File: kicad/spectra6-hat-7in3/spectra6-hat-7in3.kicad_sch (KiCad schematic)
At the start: 0 parts

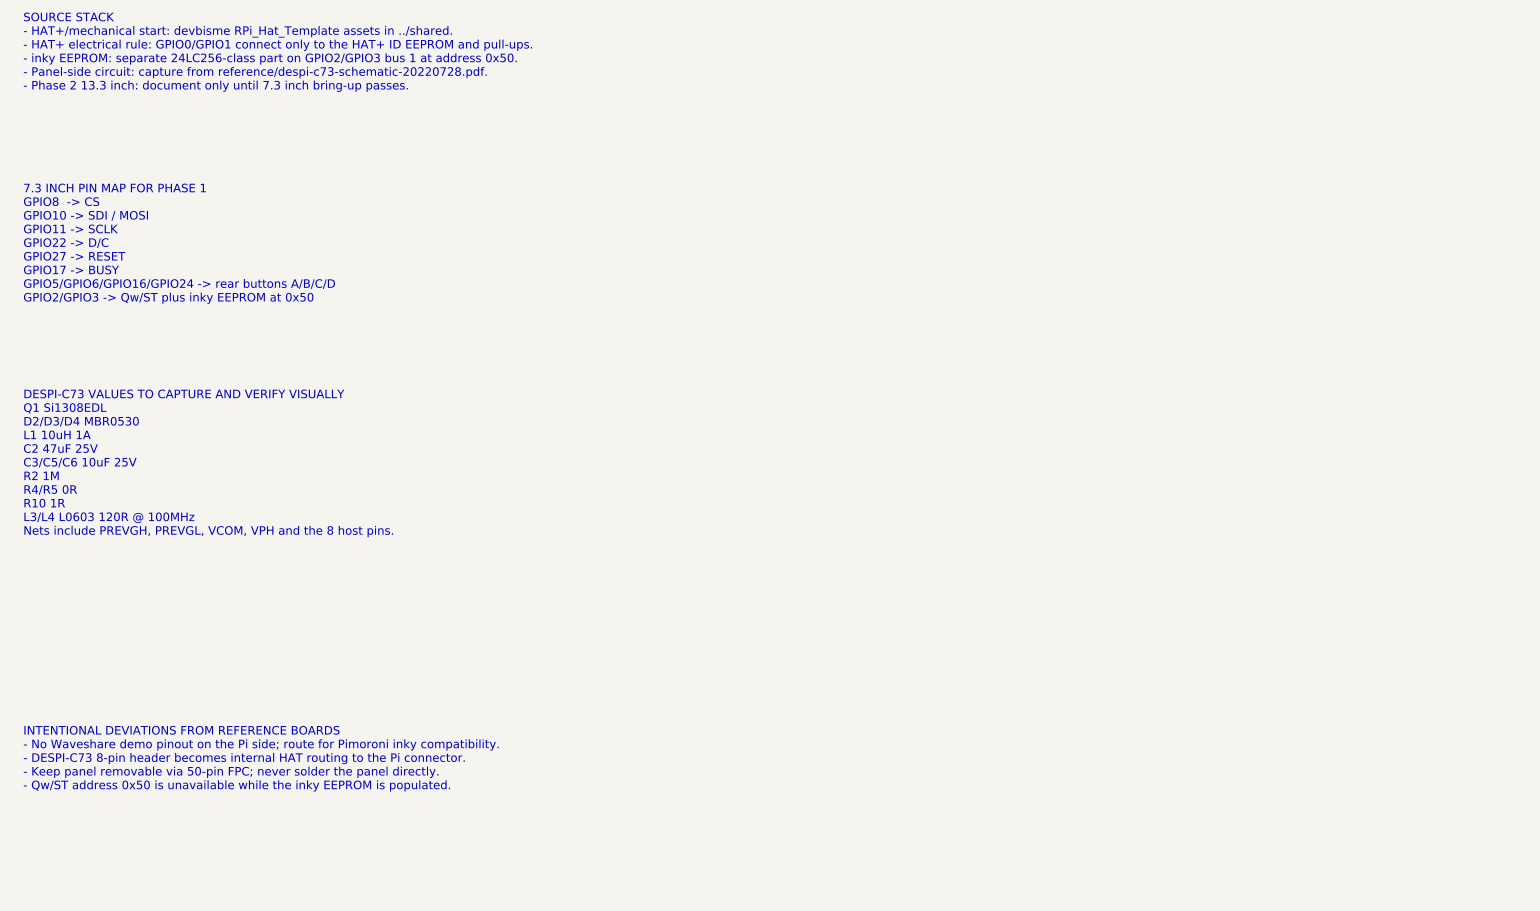
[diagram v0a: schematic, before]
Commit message: Capture Pi-side schematic blocks
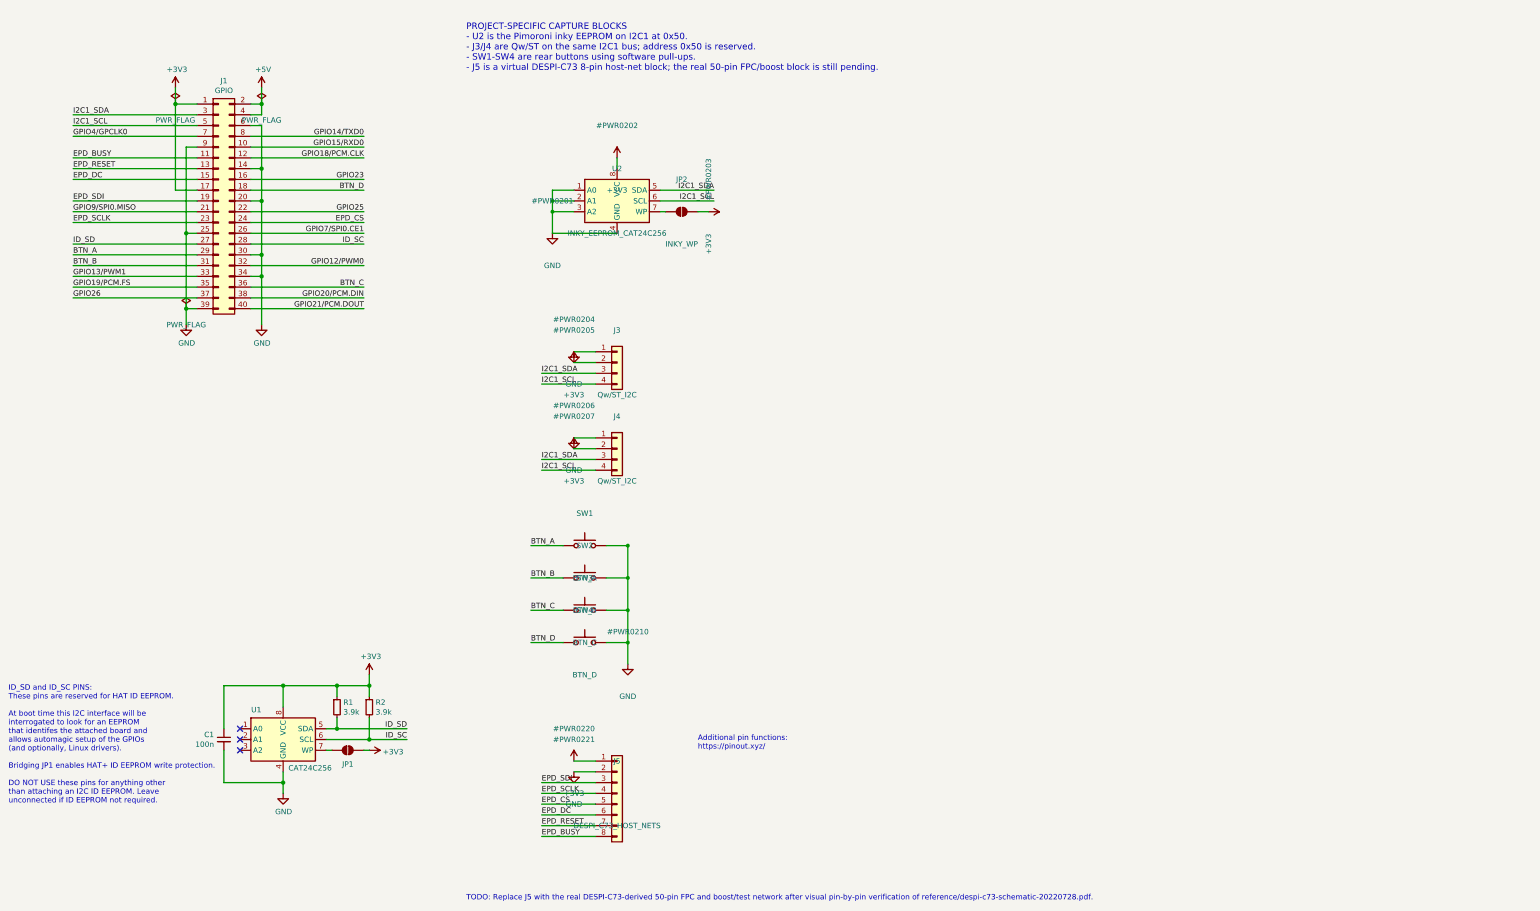
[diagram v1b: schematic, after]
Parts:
- added C1: 100n, symbol Device:C_Small
- added J1: GPIO, Connector_PinSocket_2.54mm:PinSocket_2x20_P2.54mm_Vertical, symbol Connector_Generic:Conn_02x20_Odd_Even
- added J3, J4: Qw/ST_I2C, Connector_JST:JST_SH_SM04B-SRSS-TB_1x04-1MP_P1.00mm_Horizontal, symbol Connector_Generic:Conn_01x04
- added J5: DESPI_C73_HOST_NETS, symbol Connector_Generic:Conn_01x08
- added JP1: ID_WP, symbol Jumper:SolderJumper_2_Open
- added JP2: INKY_WP, Jumper:SolderJumper-2_P1.3mm_Open_TrianglePad1.0x1.5mm, symbol Jumper:SolderJumper_2_Open
- added R1, R2: 3.9k, symbol Device:R_Small
- added SW1: BTN_A, symbol Switch:SW_Push
- added SW2: BTN_B, symbol Switch:SW_Push
- added SW3: BTN_C, symbol Switch:SW_Push
- added SW4: BTN_D, symbol Switch:SW_Push
- added U1: CAT24C256, symbol Memory_EEPROM:CAT24C256
- added U2: INKY_EEPROM_CAT24C256, Package_SO:SOIC-8_3.9x4.9mm_P1.27mm, symbol Memory_EEPROM:CAT24C256
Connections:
- new net: JP1.1 (A), U1.7 (WP)
- new net: JP2.1 (A), U2.7 (WP)
- new net +3V3: C1.1, J1.1 (Pin_1), J1.17 (Pin_17), J3.2 (Pin_2), J4.2 (Pin_2), J5.1 (Pin_1), JP1.2 (B), JP2.2 (B), R1.1, R2.1, U1.8 (VCC), U2.8 (VCC)
- new net +5V: J1.2 (Pin_2), J1.4 (Pin_4)
- new net BTN_A: J1.29 (Pin_29), SW1.1
- new net BTN_B: J1.31 (Pin_31), SW2.1
- new net BTN_C: J1.36 (Pin_36), SW3.1
- new net BTN_D: J1.18 (Pin_18), SW4.1
- new net EPD_BUSY: J1.11 (Pin_11), J5.8 (Pin_8)
- new net EPD_CS: J1.24 (Pin_24), J5.5 (Pin_5)
- new net EPD_DC: J1.15 (Pin_15), J5.6 (Pin_6)
- new net EPD_RESET: J1.13 (Pin_13), J5.7 (Pin_7)
- new net EPD_SCLK: J1.23 (Pin_23), J5.4 (Pin_4)
- new net EPD_SDI: J1.19 (Pin_19), J5.3 (Pin_3)
- new net GND: C1.2, J1.14 (Pin_14), J1.20 (Pin_20), J1.25 (Pin_25), J1.30 (Pin_30), J1.34 (Pin_34), J1.39 (Pin_39), J1.6 (Pin_6), J1.9 (Pin_9), J3.1 (Pin_1), J4.1 (Pin_1), J5.2 (Pin_2), SW1.2, SW2.2, SW3.2, SW4.2, U1.4 (GND), U2.1 (A0), U2.2 (A1), U2.3 (A2), U2.4 (GND)
- new net GPIO12/PWM0: J1.32 (Pin_32)
- new net GPIO13/PWM1: J1.33 (Pin_33)
- new net GPIO14/TXD0: J1.8 (Pin_8)
- new net GPIO15/RXD0: J1.10 (Pin_10)
- new net GPIO18/PCM.CLK: J1.12 (Pin_12)
- new net GPIO19/PCM.FS: J1.35 (Pin_35)
- new net GPIO20/PCM.DIN: J1.38 (Pin_38)
- new net GPIO21/PCM.DOUT: J1.40 (Pin_40)
- new net GPIO23: J1.16 (Pin_16)
- new net GPIO25: J1.22 (Pin_22)
- new net GPIO26: J1.37 (Pin_37)
- new net GPIO4/GPCLK0: J1.7 (Pin_7)
- new net GPIO7/SPI0.CE1: J1.26 (Pin_26)
- new net GPIO9/SPI0.MISO: J1.21 (Pin_21)
- new net I2C1_SCL: J1.5 (Pin_5), J3.4 (Pin_4), J4.4 (Pin_4), U2.6 (SCL)
- new net I2C1_SDA: J1.3 (Pin_3), J3.3 (Pin_3), J4.3 (Pin_3), U2.5 (SDA)
- new net ID_SC: J1.28 (Pin_28), R2.2, U1.6 (SCL)
- new net ID_SD: J1.27 (Pin_27), R1.2, U1.5 (SDA)
- no-connect marks 0 -> 3
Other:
- note added: "Additional pin functions: https://pinout.xyz/"
- note added: "ID_SD and ID_SC PINS: These pins are reserved for HAT ID EEPROM. At boot time this I2C interface will be interrogated to look for an EEPROM that identifes the attached board and allows automagic setup of the GPIOs (and optionally, Linux drivers). Bridging JP1 enables HAT+ ID EEPROM write protection. DO NOT USE these pins for anything other than attaching an I2C ID EEPROM. Leave unconnected if ID 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"
- note added: "PROJECT-SPECIFIC CAPTURE BLOCKS - U2 is the Pimoroni inky EEPROM on I2C1 at 0x50. - J3/J4 are Qw/ST on the same I2C1 bus; address 0x50 is reserved. - SW1-SW4 are rear buttons using software pull-ups. - J5 is a virtual DESPI-C73 8-pin host-net block; the real 50-pin FPC/boost block is still pending."
- note added: "TODO: Replace J5 with the real DESPI-C73-derived 50-pin FPC and boost/test network after visual pin-by-pin verification of reference/despi-c73-schematic-20220728.pdf."
- note removed: "7.3 INCH PIN MAP FOR PHASE 1 GPIO8 -> CS GPIO10 -> SDI / MOSI GPIO11 -> SCLK GPIO22 -> D/C GPIO27 -> RESET GPIO17 -> BUSY GPIO5/GPIO6/GPIO16/GPIO24 -> rear buttons A/B/C/D GPIO2/GPIO3 -> Qw/ST plus inky EEPROM at 0x50"
- note removed: "DESPI-C73 VALUES TO CAPTURE AND VERIFY VISUALLY Q1 Si1308EDL D2/D3/D4 MBR0530 L1 10uH 1A C2 47uF 25V C3/C5/C6 10uF 25V R2 1M R4/R5 0R R10 1R L3/L4 L0603 120R @ 100MHz Nets include PREVGH, PREVGL, VCOM, VPH and the 8 host pins."
- note removed: "INTENTIONAL DEVIATIONS FROM REFERENCE BOARDS - No Waveshare demo pinout on the Pi side; route for Pimoroni inky compatibility. - DESPI-C73 8-pin header becomes internal HAT routing to the Pi connector. - Keep panel removable via 50-pin FPC; never solder the panel directly. - Qw/ST address 0x50 is unavailable while the inky EEPROM is populated."
- note removed: "SOURCE STACK - HAT+/mechanical start: devbisme RPi_Hat_Template assets in ../shared. - HAT+ electrical rule: GPIO0/GPIO1 connect only to the HAT+ ID EEPROM and pull-ups. - inky EEPROM: separate 24LC256-class part on GPIO2/GPIO3 bus 1 at address 0x50. - Panel-side circuit: capture from reference/despi-c73-schematic-20220728.pdf. - Phase 2 13.3 inch: document only until 7.3 inch bring-up passes."
- title: Spectra 6 HAT 7.3 - Schematic Capture Prep -> Spectra 6 HAT 7.3 - Phase 1 Schematic

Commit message: Capture DESPI-C73 panel-side schematic
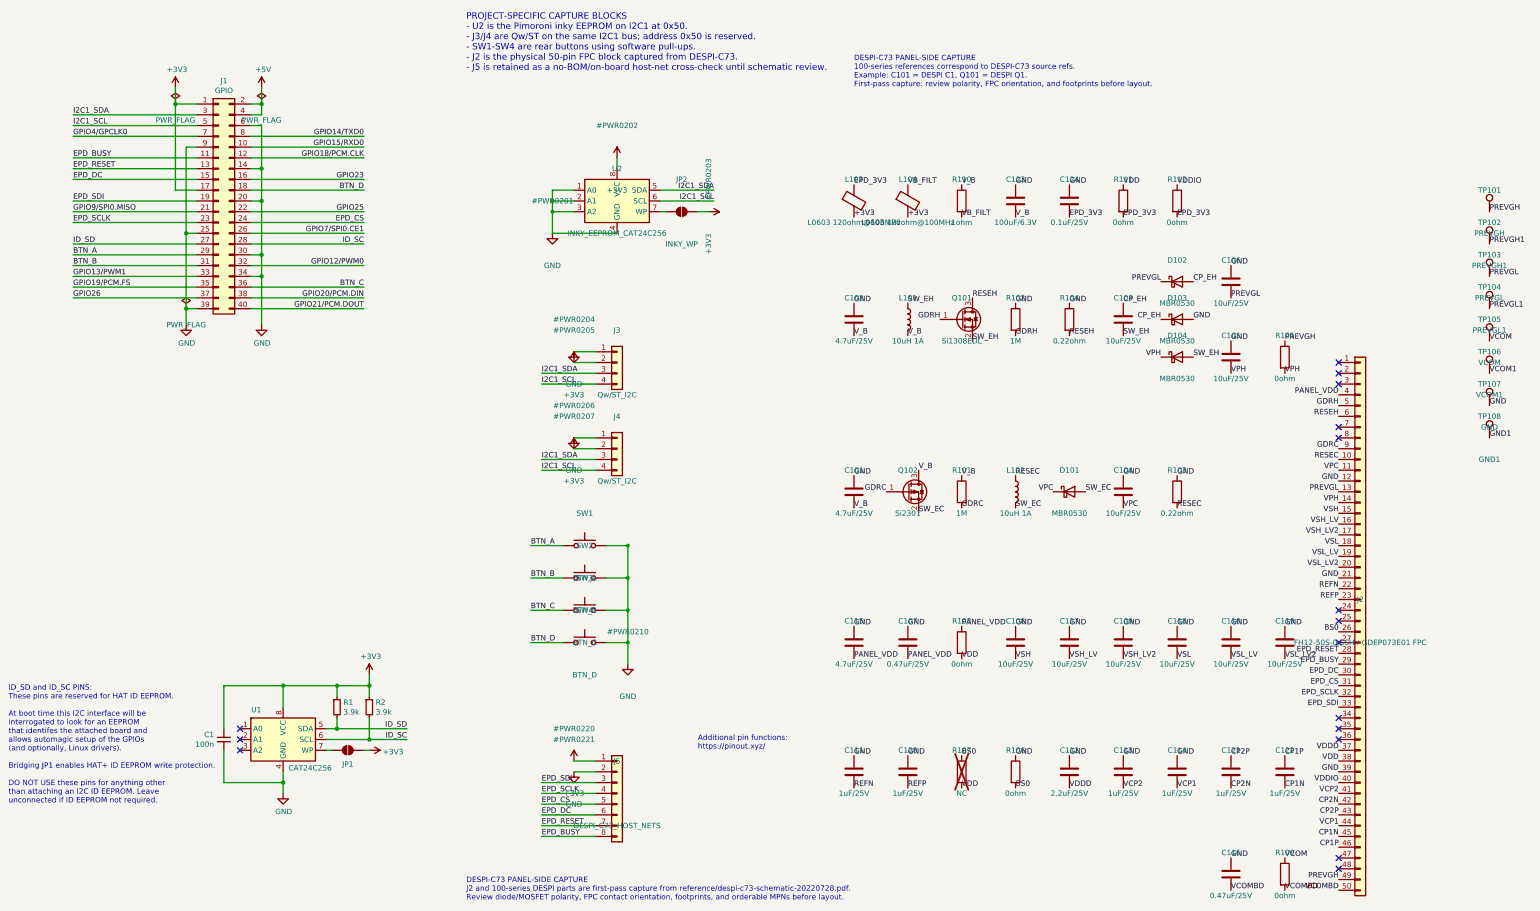
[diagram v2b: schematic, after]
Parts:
- added C101, C102, C115: 4.7uF/25V, symbol Device:C
- added C103, C104, C105, C106, C108, C109, C110, C117, C118, C119: 10uF/25V, symbol Device:C
- added C107, C116: 0.47uF/25V, symbol Device:C
- added C111, C113, C114, C120, C121, C122: 1uF/25V, symbol Device:C
- added C112: 2.2uF/25V, symbol Device:C
- added C123: 100uF/6.3V, symbol Device:C
- added C124: 0.1uF/25V, symbol Device:C
- added D101, D102, D103, D104: MBR0530, symbol Device:D_Schottky
- added J2: FH12-50S-0.5SH / GDEP073E01 FPC, Connector_FFC-FPC:Hirose_FH12-50S-0.5SH_1x50-1MP_P0.50mm_Horizontal, symbol Connector_Generic:Conn_01x50
- added L101, L102: 10uH 1A, symbol Device:L
- added L103, L104: L0603 120ohm@100MHz, symbol Device:FerriteBead
- added Q101: Si1308EDL, symbol Transistor_FET:Q_NMOS_GSD
- added Q102: Si2301, symbol Transistor_FET:Q_PMOS_GSD
- added R101, R102: 1M, symbol Device:R
- added R103, R104: 0.22ohm, symbol Device:R
- added R105, R106, R108, R109, R111, R112: 0ohm, symbol Device:R
- added R107: NC, symbol Device:R
- added R110: 1ohm, symbol Device:R
- added TP101: PREVGH, TestPoint:TestPoint_Pad_D1.0mm, symbol Connector:TestPoint
- added TP102: PREVGH1, TestPoint:TestPoint_Pad_D1.0mm, symbol Connector:TestPoint
- added TP103: PREVGL, TestPoint:TestPoint_Pad_D1.0mm, symbol Connector:TestPoint
- added TP104: PREVGL1, TestPoint:TestPoint_Pad_D1.0mm, symbol Connector:TestPoint
- added TP105: VCOM, TestPoint:TestPoint_Pad_D1.0mm, symbol Connector:TestPoint
- added TP106: VCOM1, TestPoint:TestPoint_Pad_D1.0mm, symbol Connector:TestPoint
- added TP107: GND, TestPoint:TestPoint_Pad_D1.0mm, symbol Connector:TestPoint
- added TP108: GND1, TestPoint:TestPoint_Pad_D1.0mm, symbol Connector:TestPoint
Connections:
- net +3V3: now also L103.2, L104.2
- net EPD_BUSY: now also J2.29 (Pin_29)
- net EPD_CS: now also J2.31 (Pin_31)
- net EPD_DC: now also J2.30 (Pin_30)
- net EPD_RESET: now also J2.28 (Pin_28)
- net EPD_SCLK: now also J2.32 (Pin_32)
- net EPD_SDI: now also J2.33 (Pin_33)
- net GND: now also C101.1, C102.1, C104.1, C105.1, C106.1, C107.1, C108.1, C109.1, C110.1, C111.1, C112.1, C113.1, C114.1, C115.1, C116.1, C117.1, C118.1, C119.1, C120.1, C123.1, C124.1, D103.2 (A), J2.12 (Pin_12), J2.21 (Pin_21), J2.39 (Pin_39), R102.1, R103.1, R104.1, R106.1, TP107.1
- new net BS0: J2.26 (Pin_26), R106.2, R107.1
- new net CP1N: C122.2, J2.45 (Pin_45)
- new net CP1P: C122.1, J2.46 (Pin_46)
- new net CP2N: C121.2, J2.42 (Pin_42)
- new net CP2P: C121.1, J2.43 (Pin_43)
- new net CP_EH: C103.1, D102.2 (A), D103.1 (K)
- new net EPD_3V3: C124.2, L103.1, R111.2, R112.2
- new net GDRC: J2.9 (Pin_9), Q102.1 (G), R101.2
- new net GDRH: J2.5 (Pin_5), Q101.1 (G), R102.2
- new net GND1: TP108.1
- new net PANEL_VDD: C107.2, C115.2, J2.4 (Pin_4), R108.1
- new net PREVGH: J2.49 (Pin_49), R105.1, TP101.1
- new net PREVGH1: TP102.1
- new net PREVGL: C106.2, D102.1 (K), J2.13 (Pin_13), TP103.1
- new net PREVGL1: TP104.1
- new net REFN: C111.2, J2.22 (Pin_22)
- new net REFP: C120.2, J2.23 (Pin_23)
- new net RESEC: J2.10 (Pin_10), L102.1, R103.2
- new net RESEH: J2.6 (Pin_6), Q101.3 (D), R104.2
- new net SW_EC: D101.2 (A), L102.2, Q102.2 (S)
- new net SW_EH: C103.2, D104.2 (A), L101.1, Q101.2 (S)
- new net VB_FILT: L104.1, R110.2
- new net VCOM: R109.1, TP105.1
- new net VCOM1: TP106.1
- new net VCOMBD: C116.2, J2.50 (Pin_50), R109.2
- new net VCP1: C114.2, J2.44 (Pin_44)
- new net VCP2: C113.2, J2.41 (Pin_41)
- new net VDD: J2.38 (Pin_38), R107.2, R108.2, R111.1
- new net VDDD: C112.2, J2.37 (Pin_37)
- new net VDDIO: J2.40 (Pin_40), R112.1
- new net VPC: C104.2, D101.1 (K), J2.11 (Pin_11)
- new net VPH: C105.2, D104.1 (K), J2.14 (Pin_14), R105.2
- new net VSH: C108.2, J2.15 (Pin_15)
- new net VSH_LV: C117.2, J2.16 (Pin_16)
- new net VSH_LV2: C109.2, J2.17 (Pin_17)
- new net VSL: C118.2, J2.18 (Pin_18)
- new net VSL_LV: C110.2, J2.19 (Pin_19)
- new net VSL_LV2: C119.2, J2.20 (Pin_20)
- new net V_B: C101.2, C102.2, C123.2, L101.2, Q102.3 (D), R101.1, R110.1
- no-connect marks 3 -> 16
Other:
- note added: "DESPI-C73 PANEL-SIDE CAPTURE 100-series references correspond to DESPI-C73 source refs. Example: C101 = DESPI C1, Q101 = DESPI Q1. First-pass capture: review polarity, FPC orientation, and footprints before layout."
- note added: "DESPI-C73 PANEL-SIDE CAPTURE J2 and 100-series DESPI parts are first-pass capture from reference/despi-c73-schematic-20220728.pdf. Review diode/MOSFET polarity, FPC contact orientation, footprints, and orderable MPNs before layout."
- note added: "PROJECT-SPECIFIC CAPTURE BLOCKS - U2 is the Pimoroni inky EEPROM on I2C1 at 0x50. - J3/J4 are Qw/ST on the same I2C1 bus; address 0x50 is reserved. - SW1-SW4 are rear buttons using software pull-ups. - J2 is the physical 50-pin FPC block captured from DESPI-C73. - J5 is retained as a no-BOM/on-board host-net cross-check until schematic review."
- note removed: "PROJECT-SPECIFIC CAPTURE BLOCKS - U2 is the Pimoroni inky EEPROM on I2C1 at 0x50. - J3/J4 are Qw/ST on the same I2C1 bus; address 0x50 is reserved. - SW1-SW4 are rear buttons using software pull-ups. - J5 is a virtual DESPI-C73 8-pin host-net block; the real 50-pin FPC/boost block is still pending."
- note removed: "TODO: Replace J5 with the real DESPI-C73-derived 50-pin FPC and boost/test network after visual pin-by-pin verification of reference/despi-c73-schematic-20220728.pdf."
